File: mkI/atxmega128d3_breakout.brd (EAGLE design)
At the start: 33 x 66.7 mm, 23 parts, among them U1 ATXMEGA128A3-AU

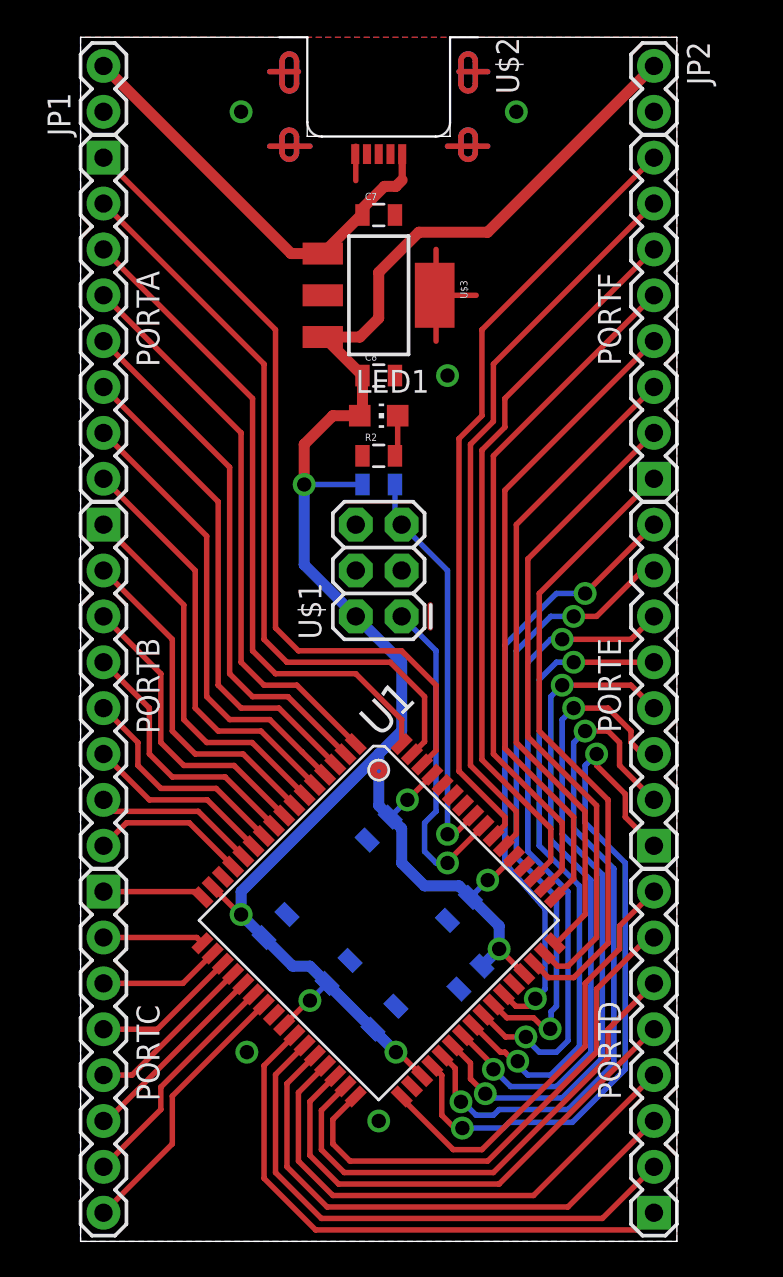
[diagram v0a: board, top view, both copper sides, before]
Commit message: pdf output of board and schematic
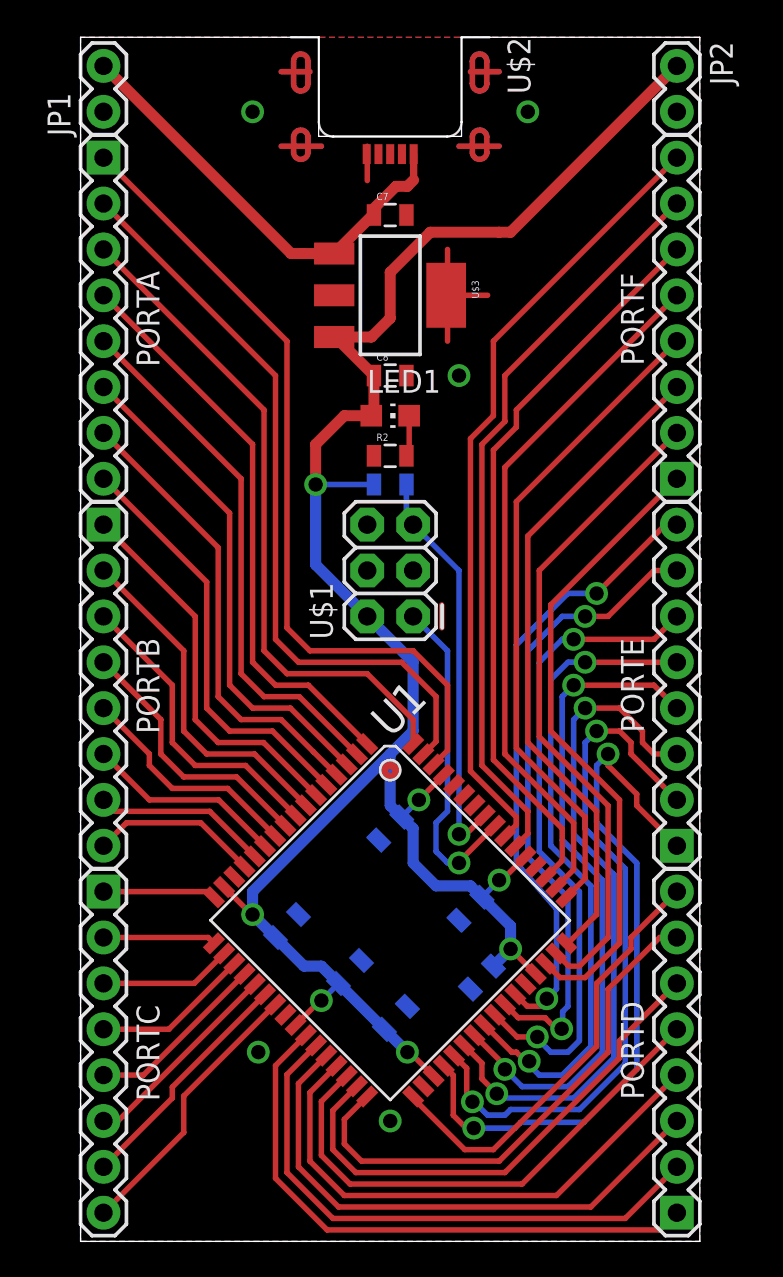
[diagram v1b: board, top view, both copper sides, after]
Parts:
- moved JP2 1.27 mm to (33.0, 65.1)
- moved PORTD 1.27 mm to (33.0, 1.59)
- moved PORTE 1.27 mm to (33.0, 21.9)
- moved PORTF 1.27 mm to (33.0, 42.2)
- moved C3 0.64 mm to (22.2, 14.6)
- moved C5 0.64 mm to (21.6, 18.4)
- moved C1 0.63 mm to (11.4, 17.5)
- moved C2 0.63 mm to (14.9, 14.9)
- moved C4 0.63 mm to (17.5, 12.4)
- moved C6 0.63 mm to (17.1, 22.9)
- moved C7 0.63 mm to (17.1, 56.8)
- moved C8 0.63 mm to (17.1, 47.9)
- moved LED1 0.63 mm to (17.1, 45.7)
- moved R1 0.63 mm to (17.1, 41.9)
- moved R2 0.63 mm to (17.1, 43.5)
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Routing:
- net RAW: track 24.2 -> 24.8 mm
- net PE7: track 33.8 -> 34.5 mm
- net PE6: track 35.1 -> 35.8 mm
- net PE3: track 36.3 -> 36.9 mm
- net PD3: track 29.1 -> 29.8 mm
- net PD2: track 30.0 -> 30.6 mm
- net PD1: track 30.9 -> 31.5 mm
- net PD6: track 28.5 -> 29.1 mm
- net PD4: track 28.2 -> 28.9 mm
- net PD0: track 31.8 -> 32.4 mm
- net PB6: track 9.04 -> 9.68 mm
- net PC1: track 5.61 -> 6.25 mm
- net PC5: track 10.9 -> 11.5 mm
- net PC4: track 9.50 -> 10.1 mm
- net PC3: track 8.12 -> 8.75 mm
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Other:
- board size 33 x 66.7 mm -> 34.3 x 66.7 mm
